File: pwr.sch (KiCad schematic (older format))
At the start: 57 parts, among them U1 FT601, U10 MIC94310, U11 PAM2305, U4 ECP5, U6 PAM2305, U7 NCP186, U8 MIC94310, U9 MIC94310, X2 CONN_01X08

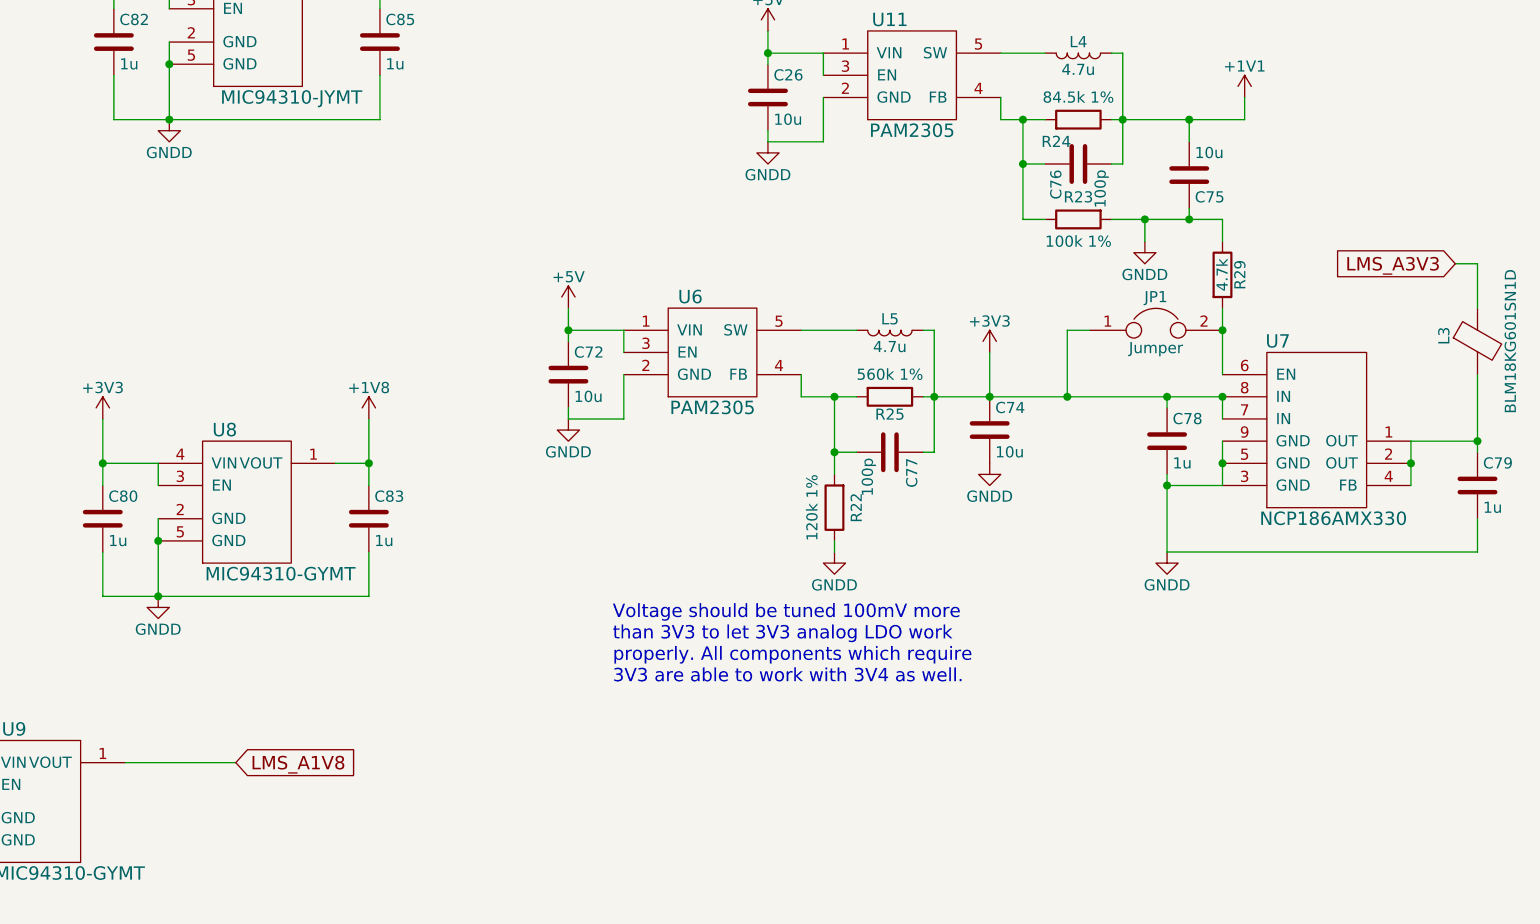
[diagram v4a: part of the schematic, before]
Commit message: Fix LMS_3V3A enable pull. Corrected shield ground
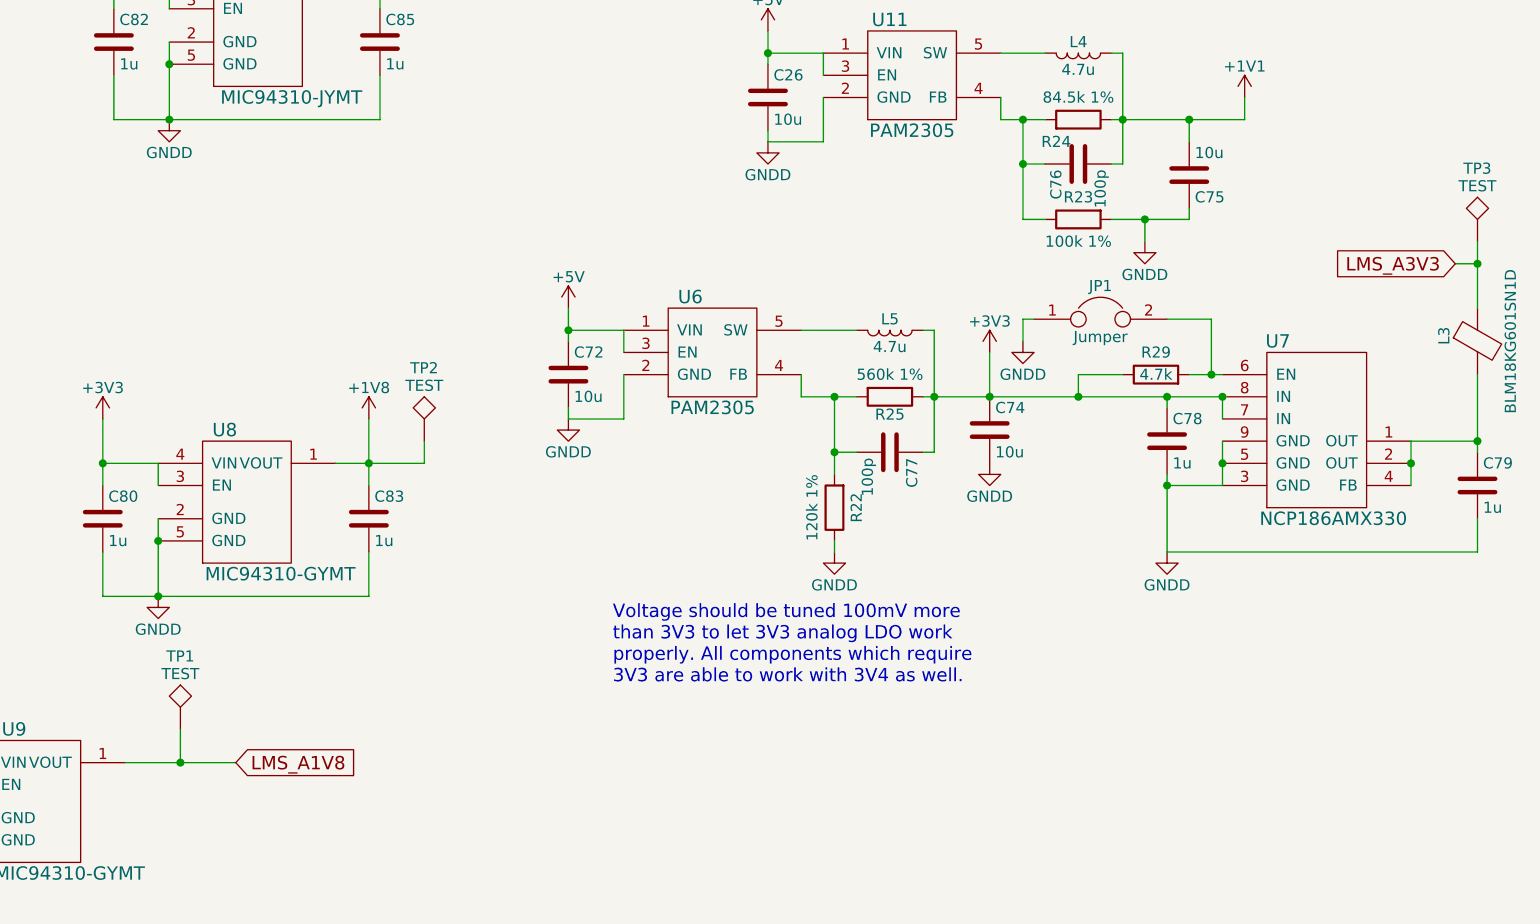
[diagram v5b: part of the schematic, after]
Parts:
- added TP1, TP2, TP3: TEST, Measurement_Points:Measurement_Point_Square-SMD-Pad_Small, symbol TEST
- JP1, JP2: footprint Pin_Headers:Pin_Header_Straight_1x02_Pitch2.54mm -> Pin_Headers:Pin_Header_Angled_1x02_Pitch2.54mm
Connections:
- net +1V8: now also TP2.1
- net +3V3: now also R29.1; no longer JP1.1
- net GNDD: now also JP1.1; no longer R29.1
- net LMS_A1V8: now also TP1.1
- net LMS_A3V3: now also TP3.1
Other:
- moved on the sheet: JP1, R29
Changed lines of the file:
@@
 $Descr A4 11693 8268
 encoding utf-8
-Sheet 2 6
+Sheet 2 7
 Title "SDR"
 Date ""
@@
 	5850 5300 5850 5600
 Wire Wire Line
-	5850 5500 5700 5500
+	5700 5500 6100 5500
 $Comp
 L C C80
@@
 	9550 3950 9550 4050
 Wire Wire Line
-	9200 4400 9700 4400
+	9200 4400 9550 4400
 Wire Wire Line
 	9350 4400 9350 4500
@@
 	10850 5100 10850 5450
 Wire Wire Line
-	10850 4600 10850 4800
+	10850 4500 10850 4800
 NoConn ~ 9850 2650
 $Comp
 L Jumper JP1
 U 1 1 59327579
-P 9400 4900
-F 0 "JP1" H 9400 5050 50  0000 C CNN
-F 1 "Jumper" H 9400 4820 50  0000 C CNN
-F 2 "Pin_Headers:Pin_Header_Straight_1x02_Pitch2.54mm" H 9400 4900 50  0001 C CNN
-F 3 "" H 9400 4900 50  0001 C CNN
-	1    9400 4900
+P 9150 4850
+F 0 "JP1" H 9150 5000 50  0000 C CNN
+F 1 "Jumper" H 9150 4770 50  0000 C CNN
+F 2 "Pin_Headers:Pin_Header_Angled_1x02_Pitch2.54mm" H 9150 4850 50  0001 C CNN
+F 3 "" H 9150 4850 50  0001 C CNN
+	1    9150 4850
 	1    0    0    -1
 $EndComp
 Connection ~ 9450 5200
 Wire Wire Line
-	9700 4800 9700 5100
-Wire Wire Line
 	10850 4600 10750 4600
-Wire Wire Line
-	9100 4900 9000 4900
-Wire Wire Line
-	9000 4900 9000 5200
-Connection ~ 9000 5200
 $Comp
 L R R29
 U 1 1 593281E5
-P 9700 4650
-F 0 "R29" V 9780 4650 50  0000 C CNN
-F 1 "4.7k" V 9700 4650 50  0000 C CNN
-F 2 "Resistors_SMD:R_0603" V 9630 4650 50  0001 C CNN
-F 3 "" H 9700 4650 50  0001 C CNN
-	1    9700 4650
-	1    0    0    -1
-$EndComp
-Connection ~ 9700 4900
-Wire Wire Line
-	9700 4400 9700 4500
-Connection ~ 9550 4400
+P 9400 5100
+F 0 "R29" V 9500 5100 50  0000 C CNN
+F 1 "4.7k" V 9400 5100 50  0000 C CNN
+F 2 "Resistors_SMD:R_0603" V 9330 5100 50  0001 C CNN
+F 3 "" H 9400 5100 50  0001 C CNN
+	1    9400 5100
+	0    -1   -1   0
+$EndComp
 $Comp
 L Jumper JP2
@@
 F 0 "JP2" H 3700 1550 50  0000 C CNN
 F 1 "Jumper" H 3700 1320 50  0000 C CNN
-F 2 "Pin_Headers:Pin_Header_Straight_1x02_Pitch2.54mm" H 3700 1400 50  0001 C CNN
+F 2 "Pin_Headers:Pin_Header_Angled_1x02_Pitch2.54mm" H 3700 1400 50  0001 C CNN
 F 3 "" H 3700 1400 50  0001 C CNN
 	1    3700 1400
@@
 	4050 1600 4050 1400
 Connection ~ 4050 1400
+$Comp
+L TEST TP3
+U 1 1 59339CA4
+P 10850 4500
+F 0 "TP3" H 10850 4800 50  0000 C BNN
+F 1 "TEST" H 10850 4750 50  0000 C CNN
+F 2 "Measurement_Points:Measurement_Point_Square-SMD-Pad_Small" H 10850 4500 50  0001 C CNN
+F 3 "" H 10850 4500 50  0001 C CNN
+	1    10850 4500
+	1    0    0    -1
+$EndComp
+Connection ~ 10850 4600
+$Comp
+L TEST TP1
+U 1 1 5933A8A7
+P 5000 6700
+F 0 "TP1" H 5000 7000 50  0000 C BNN
+F 1 "TEST" H 5000 6950 50  0000 C CNN
+F 2 "Measurement_Points:Measurement_Point_Square-SMD-Pad_Small" H 5000 6700 50  0001 C CNN
+F 3 "" H 5000 6700 50  0001 C CNN
+	1    5000 6700
+	1    0    0    -1
+$EndComp
+Wire Wire Line
+	5000 6700 5000 6850
+Connection ~ 5000 6850
+$Comp
+L TEST TP2
+U 1 1 5933AA96
+P 6100 5400
+F 0 "TP2" H 6100 5700 50  0000 C BNN
+F 1 "TEST" H 6100 5650 50  0000 C CNN
+F 2 "Measurement_Points:Measurement_Point_Square-SMD-Pad_Small" H 6100 5400 50  0001 C CNN
+F 3 "" H 6100 5400 50  0001 C CNN
+	1    6100 5400
+	1    0    0    -1
+$EndComp
+Wire Wire Line
+	6100 5500 6100 5400
+Wire Wire Line
+	9700 5100 9550 5100
+Wire Wire Line
+	9450 4850 9650 4850
+Wire Wire Line
+	9650 4850 9650 5100
+Connection ~ 9650 5100
+$Comp
+L GNDD #PWR037
+U 1 1 5936655F
+P 8800 4950
+F 0 "#PWR037" H 8800 4700 50  0001 C CNN
+F 1 "GNDD" H 8800 4800 50  0000 C CNN
+F 2 "" H 8800 4950 50  0000 C CNN
+F 3 "" H 8800 4950 50  0000 C CNN
+	1    8800 4950
+	-1   0    0    -1
+$EndComp
+Wire Wire Line
+	8800 4950 8800 4850
+Wire Wire Line
+	8800 4850 8850 4850
+Wire Wire Line
+	9250 5100 9050 5100
+Wire Wire Line
+	9050 5100 9050 5200
+Connection ~ 9050 5200
 $EndSCHEMATC

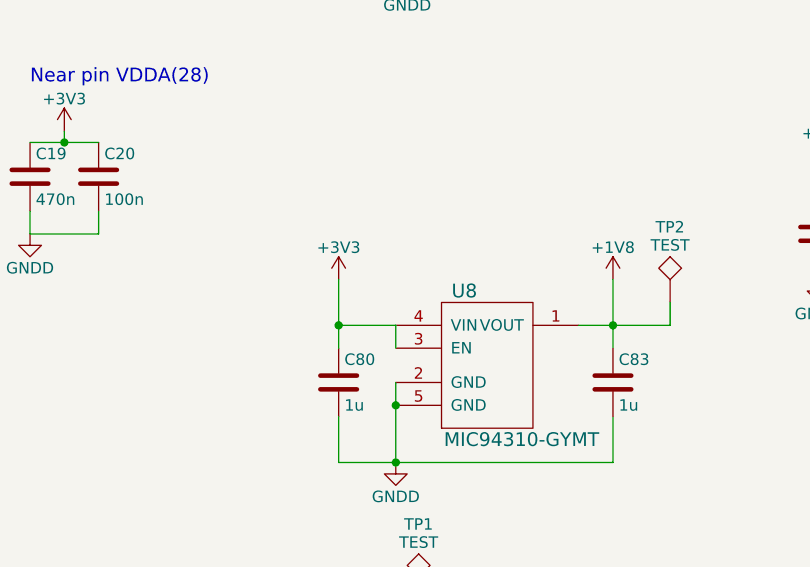
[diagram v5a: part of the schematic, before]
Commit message: Add schematic of FT232H. Not placed yet.
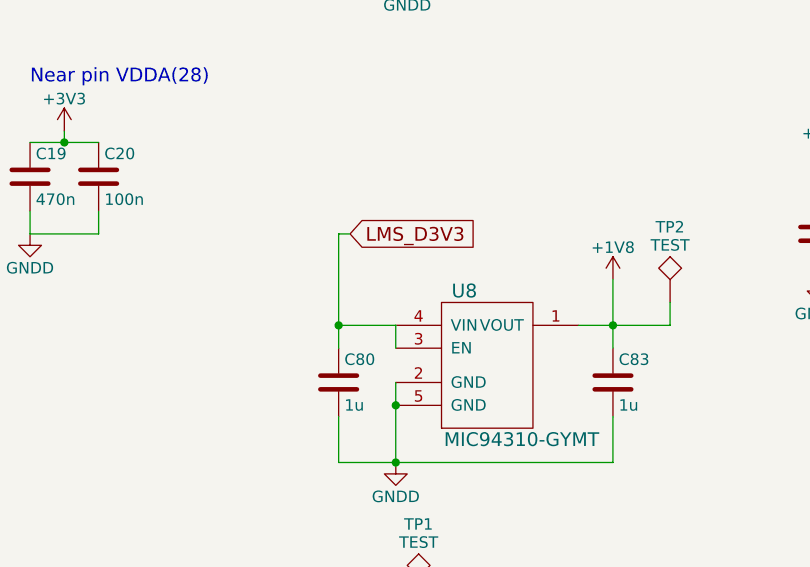
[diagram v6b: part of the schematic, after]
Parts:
- L3: footprint Capacitors_SMD:C_0805 -> Inductors_SMD:L_0805
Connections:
- net +3V3: no longer C80.1, U8.3 (EN), U8.4 (VIN)
- net LMS_D3V3: now also C80.1, U8.3 (EN), U8.4 (VIN)
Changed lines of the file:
@@
 $EndComp
 Wire Wire Line
-	4650 5300 4650 5600
+	4650 5100 4650 5600
 Wire Wire Line
 	4900 5500 4650 5500
@@
 	4650 5900 4650 6100
 Connection ~ 4900 6100
-$Comp
-L +3V3 #PWR025
-U 1 1 58A7AA68
-P 4650 5300
-F 0 "#PWR025" H 4650 5150 50  0001 C CNN
-F 1 "+3V3" H 4650 5440 50  0000 C CNN
-F 2 "" H 4650 5300 50  0000 C CNN
-F 3 "" H 4650 5300 50  0000 C CNN
-	1    4650 5300
-	1    0    0    -1
-$EndComp
 Connection ~ 4650 5500
 $Comp
@@
 F 0 "L3" V 10700 4975 50  0000 C CNN
 F 1 "BLM18KG601SN1D" V 11000 4950 50  0000 C CNN
-F 2 "Capacitors_SMD:C_0805" V 10780 4950 50  0001 C CNN
+F 2 "Inductors_SMD:L_0805" V 10780 4950 50  0001 C CNN
 F 3 "" H 10850 4950 50  0000 C CNN
 	1    10850 4950
@@
 	9050 5100 9050 5200
 Connection ~ 9050 5200
+Text GLabel 4700 5100 2    60   Input ~ 0
+LMS_D3V3
+Wire Wire Line
+	4650 5100 4700 5100
 $EndSCHEMATC
